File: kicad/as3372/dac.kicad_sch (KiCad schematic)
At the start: 6 parts, among them U13 LM4040AIM3-2.5, U14 AD5328

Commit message: incremental updates
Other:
- title: Zoxnoxious 3340 Oscillator -> Z3372 Signal Processing
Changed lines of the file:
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@@
   (paper "B")
   (title_block
-    (title "Zoxnoxious 3340 Oscillator")
-    (rev "0.4")
+    (title "Z3372 Signal Processing")
+    (rev "0.1")
     (company "Zoxnoxious Engineering")
   )

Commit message: progress
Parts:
- added C? (x2): 1n, Capacitor_SMD:C_0603_1608Metric, symbol Device:C
- added R? (x2): 2.4k, Resistor_SMD:R_0603_1608Metric, symbol Device:R
- added R? (x2): 120k, Resistor_SMD:R_0603_1608Metric, symbol Device:R
- added R? (x2): 3.3k, Resistor_SMD:R_0603_1608Metric, symbol Device:R
- added R? (x2): 8.2k, Resistor_SMD:R_0603_1608Metric, symbol Device:R
- added U? (x3): TL072, symbol Amplifier_Operational:TL072
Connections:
- net GND: now also C?.2, C?.2, R?.1, R?.1
- net VREF_2.5V: now also R?.1, R?.1
- net VCF_CV: now reaches U14.10 (VOUT_E)
- net VCF_CV: now also R?.1
- net PAN_VCA_CV: now reaches U14.11 (VOUT_F)
- net PAN_VCA_CV: now also R?.1
- net SIG1_VCA1_CV: now reaches U14.4 (VOUT_A)
- net SIG2_VCA2_CV: now reaches U14.5 (VOUT_B)
- net MOD_AMOUNT_VCA3_CV: now reaches U14.6 (VOUT_C)
- net RESONANCE_CV: now reaches U14.7 (VOUT_D)
- new net: C?.1, R?.2, R?.2, U?.5 (+)
- new net: R?.1, R?.2, U?.2 (-)
- new net: R?.2, U?.1
- new net: C?.1, R?.2, R?.2, U?.3 (+)
- new net: R?.1, R?.2, U?.6 (-)
- new net: R?.2, U?.7
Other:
- note added: "ADD SIMPLE RC FILTERING HERE"
- note added: "Control Voltage levels: Sig1 VCA CV: 0-5V Sig2 VCA CV: 0-5V VCA Mod Level CV: 0-5V Res CV: 0-5V VCF CV: -1 - +6V Pan VCA CV: -1 - +6V The latter two use opamps to scale; everything else can be straight from DAC"
- note added: "LM4040 resistor rough calc: Ilm4040 min: 70uA Vref input impedance: 10M"
- note removed: "LM4040 resistor rough calc: Ilm4040 min: 70uA Rdacref = 100k ==> I = 25uA opamp will swing about 0 ~{50} uA for roughly 150uA ==> 16kR min Lower to 5k, call it good"
- moved on the sheet: C24, C25, C39, R47, U13, U14

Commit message: daily update
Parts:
- removed U14: AD5328, Package_SO:TSSOP-16_4.4x5mm_P0.65mm, symbol as3340:AD5328
- removed U? (x3): TL072, symbol Amplifier_Operational:TL072
- added C7, C8: 0.1u, Capacitor_SMD:C_0603_1608Metric, symbol Device:C
- added TP14: TestPoint, symbol Connector:TestPoint
- added U4: TL074, symbol Amplifier_Operational:TL074
- added U9: AD5328, Package_SO:TSSOP-16_4.4x5mm_P0.65mm, symbol as3372_lib:AD5328
- C10, C9: renamed from C?; value 1n -> 68n; LCSC Part (none) -> C31658
- gave numbers to parts that had none: 8
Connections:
- net +5V: now also U9.3 (VDD)
- net DIN: now also U9.15 (DIN)
- net GND: now also C7.1, C8.1, U4.12 (+), U9.1 (~{LDAC}), U9.14 (GND)
- net MOD_AMOUNT_VCA3_CV: now also U9.6 (VOUT_C)
- net PAN_VCA_CV: now also R12.2, U4.1; no longer R6.1
- net RESONANCE_CV: now also U9.7 (VOUT_D)
- net SCLK: now also U9.16 (SCLK)
- net SIG1_VCA1_CV: now also U9.4 (VOUT_A)
- net SIG2_VCA2_CV: now also U9.5 (VOUT_B)
- net VCF_CV: now also R11.2, U4.7; no longer R5.1
- net VREF_2.5V: now also U4.10 (+), U9.8 (VREF_ABCD), U9.9 (VREF_EFGH); no longer R7.1, R8.1
- net ~{DAC_CS}: now also U9.2 (~{SYNC})
- net at C10.1, R10.2, R6.2: now also U4.3 (+)
- net at R11.1, R7.2: now also U4.6 (-)
- net at C9.1, R5.2, R9.2: now also U4.5 (+)
- net at R12.1, R8.2: now also U4.2 (-)
- new net: U4.13 (-), U4.14
- new net +12V: C7.2, U4.4 (V+)
- new net -12V: C8.2, U4.11 (V-)
- new net DAC_TEST: TP14.1, U9.13 (VOUT_H)
- new net PAN_VCA_CV_0-5: R6.1, U9.11 (VOUT_F)
- new net VCF_CV_0-5: R5.1, U9.10 (VOUT_E)
- new net VREF_2.5V_BUFFERED: R7.1, R8.1, U4.8, U4.9 (-)
- no-connect marks 0 -> 1
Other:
- note added: "Decoupling"
- note added: "Differential amplifier to take 0V : 5V to -1V : 6V 68nF cap to give a ~1kHz low pass filter"
- note added: "LM4040 resistor rough calc: Ilm4040 min: 70uA Vref input impedance: 10M (buffered)"
- note added: "Unused"
- note removed: "LM4040 resistor rough calc: Ilm4040 min: 70uA Vref input impedance: 10M"
- moved on the sheet: C10, C9, R10, R11, R12, R5, R6, R7, R8, R9

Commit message: schematic updates
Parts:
- R10, R9: LCSC Part (none) -> C25808
- R11, R12: LCSC Part (none) -> C22978
- R5, R6: LCSC Part (none) -> C22940
- R7, R8: LCSC Part (none) -> C25981
- TP14: footprint (none) -> TestPoint:TestPoint_Pad_2.0x2.0mm
- U4: footprint (none) -> Package_SO:SOIC-14_3.9x8.7mm_P1.27mm; LCSC Part (none) -> C6963
- U9: LCSC Part (none) -> C29162
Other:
- note added: "AD5328: "B" version works fine. DAC: 2.5V Reference Voltage B, C, D grades of LM4040 are likely good 'nuff"
- note removed: "DAC: 2.5V Reference Voltage B, C, D grades of LM4040 are likely good 'nuff"
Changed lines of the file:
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@@
     (effects (font (size 1.27 1.27)) (justify left bottom))
   )
-  (text "DAC: 2.5V Reference Voltage\nB, C, D grades of LM4040 are likely good 'nuff"
-    (at 24.765 24.13 0)
+  (text "AD5328: \"B\" version works fine.\nDAC: 2.5V Reference Voltage\nB, C, D grades of LM4040 are likely good 'nuff"
+    (at 24.765 27.305 0)
     (effects (font (size 1.27 1.27)) (justify left bottom))
   )
@@
     )
     (property "Datasheet" "https://www.analog.com/en/products/ad5308.html" (id 3) (at 76.2 57.15 0)
+      (effects (font (size 1.27 1.27)) hide)
+    )
+    (property "LCSC Part" "C29162" (id 4) (at 76.2 57.15 0)
       (effects (font (size 1.27 1.27)) hide)
     )
@@
       (effects (font (size 1.27 1.27)) (justify right))
     )
-    (property "Footprint" "" (id 2) (at 64.77 238.76 0)
+    (property "Footprint" "Package_SO:SOIC-14_3.9x8.7mm_P1.27mm" (id 2) (at 64.77 238.76 0)
       (effects (font (size 1.27 1.27)) hide)
     )
     (property "Datasheet" "http://www.ti.com/lit/ds/symlink/tl071.pdf" (id 3) (at 62.23 236.22 0)
+      (effects (font (size 1.27 1.27)) hide)
+    )
+    (property "LCSC Part" "C6963" (id 4) (at 63.5 241.3 0)
       (effects (font (size 1.27 1.27)) hide)
     )
@@
       (effects (font (size 1.27 1.27)) hide)
     )
+    (property "LCSC Part" "C22940" (id 4) (at 185.42 149.86 0)
+      (effects (font (size 1.27 1.27)) hide)
+    )
     (pin "1")
     (pin "2")
@@
     )
     (property "Datasheet" "~" (id 3) (at 190.5 157.48 0)
+      (effects (font (size 1.27 1.27)) hide)
+    )
+    (property "LCSC Part" "C25808" (id 4) (at 190.5 157.48 0)
       (effects (font (size 1.27 1.27)) hide)
     )
@@
       (effects (font (size 1.27 1.27)) hide)
     )
+    (property "LCSC Part" "C22978" (id 4) (at 207.01 90.17 0)
+      (effects (font (size 1.27 1.27)) hide)
+    )
     (pin "1")
     (pin "2")
@@
     (property "Reference" "U4" (id 0) (at 207.01 94.0902 0))
     (property "Value" "TL074" (id 1) (at 207.01 96.6271 0))
-    (property "Footprint" "" (id 2) (at 205.74 105.41 0)
+    (property "Footprint" "Package_SO:SOIC-14_3.9x8.7mm_P1.27mm" (id 2) (at 205.74 105.41 0)
       (effects (font (size 1.27 1.27)) hide)
     )
     (property "Datasheet" "http://www.ti.com/lit/ds/symlink/tl071.pdf" (id 3) (at 208.28 107.95 0)
+      (effects (font (size 1.27 1.27)) hide)
+    )
+    (property "LCSC Part" "C6963" (id 4) (at 207.01 102.87 0)
       (effects (font (size 1.27 1.27)) hide)
     )
@@
       (effects (font (size 1.27 1.27)) hide)
     )
+    (property "LCSC Part" "C25981" (id 4) (at 189.23 100.33 0)
+      (effects (font (size 1.27 1.27)) hide)
+    )
     (pin "1")
     (pin "2")
@@
     (property "Reference" "U4" (id 0) (at 205.74 58.5302 0))
     (property "Value" "TL074" (id 1) (at 205.74 61.0671 0))
-    (property "Footprint" "" (id 2) (at 204.47 69.85 0)
+    (property "Footprint" "Package_SO:SOIC-14_3.9x8.7mm_P1.27mm" (id 2) (at 204.47 69.85 0)
       (effects (font (size 1.27 1.27)) hide)
     )
     (property "Datasheet" "http://www.ti.com/lit/ds/symlink/tl071.pdf" (id 3) (at 207.01 72.39 0)
+      (effects (font (size 1.27 1.27)) hide)
+    )
+    (property "LCSC Part" "C6963" (id 4) (at 205.74 67.31 0)
       (effects (font (size 1.27 1.27)) hide)
     )
@@
     (property "Reference" "U4" (id 0) (at 383.54 200.7702 0))
     (property "Value" "TL074" (id 1) (at 383.54 203.3071 0))
-    (property "Footprint" "" (id 2) (at 382.27 212.09 0)
+    (property "Footprint" "Package_SO:SOIC-14_3.9x8.7mm_P1.27mm" (id 2) (at 382.27 212.09 0)
       (effects (font (size 1.27 1.27)) hide)
     )
     (property "Datasheet" "http://www.ti.com/lit/ds/symlink/tl071.pdf" (id 3) (at 384.81 214.63 0)
+      (effects (font (size 1.27 1.27)) hide)
+    )
+    (property "LCSC Part" "C6963" (id 4) (at 383.54 209.55 0)
       (effects (font (size 1.27 1.27)) hide)
     )
@@
     (property "Reference" "U4" (id 0) (at 207.01 138.5402 0))
     (property "Value" "TL074" (id 1) (at 207.01 141.0771 0))
-    (property "Footprint" "" (id 2) (at 205.74 149.86 0)
+    (property "Footprint" "Package_SO:SOIC-14_3.9x8.7mm_P1.27mm" (id 2) (at 205.74 149.86 0)
       (effects (font (size 1.27 1.27)) hide)
     )
     (property "Datasheet" "http://www.ti.com/lit/ds/symlink/tl071.pdf" (id 3) (at 208.28 152.4 0)
+      (effects (font (size 1.27 1.27)) hide)
+    )
+    (property "LCSC Part" "C6963" (id 4) (at 207.01 147.32 0)
       (effects (font (size 1.27 1.27)) hide)
     )
@@
       (effects (font (size 1.27 1.27)) hide)
     )
+    (property "LCSC Part" "C22978" (id 4) (at 207.01 134.62 0)
+      (effects (font (size 1.27 1.27)) hide)
+    )
     (pin "1")
     (pin "2")
@@
       (effects (font (size 1.27 1.27)) (justify left))
     )
-    (property "Footprint" "" (id 2) (at 105.41 72.39 0)
+    (property "Footprint" "TestPoint:TestPoint_Pad_2.0x2.0mm" (id 2) (at 105.41 72.39 0)
       (effects (font (size 1.27 1.27)) hide)
     )
@@
       (effects (font (size 1.27 1.27)) hide)
     )
+    (property "LCSC Part" "C22940" (id 4) (at 185.42 105.41 0)
+      (effects (font (size 1.27 1.27)) hide)
+    )
     (pin "1")
     (pin "2")
@@
       (effects (font (size 1.27 1.27)) hide)
     )
+    (property "LCSC Part" "C25808" (id 4) (at 190.5 113.03 0)
+      (effects (font (size 1.27 1.27)) hide)
+    )
     (pin "1")
     (pin "2")
@@
       (effects (font (size 1.27 1.27)) hide)
     )
+    (property "LCSC Part" "C25981" (id 4) (at 189.23 144.78 0)
+      (effects (font (size 1.27 1.27)) hide)
+    )

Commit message: start placing
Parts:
- added C41, C42, C43, C44: 10n, Capacitor_SMD:C_0603_1608Metric, symbol Device:C
- added R74, R75, R76, R77: 15k, Resistor_SMD:R_0603_1608Metric, symbol Device:R
- C10: value 68n -> 8.2p; LCSC Part C31658 -> C1685
- R10: value 120k -> 20k; LCSC Part C25808 -> C4184
- R12: value 3.3k -> 20k; LCSC Part C22978 -> C4184
- R6: value 2.4k -> 20k; LCSC Part C22940 -> C4184
- R8: value 8.2k -> 20k; LCSC Part C25981 -> C4184
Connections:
- net GND: now also C41.2, C42.2, C43.2, C44.2
- net MOD_AMOUNT_VCA3_CV: now also C43.1, R76.2; no longer U9.6 (VOUT_C)
- net RESONANCE_CV: now also C44.1, R77.2; no longer U9.7 (VOUT_D)
- net SIG1_VCA1_CV: now also C41.1, R74.2; no longer U9.4 (VOUT_A)
- net SIG2_VCA2_CV: now also C42.1, R75.2; no longer U9.5 (VOUT_B)
- net PAN_VCA_CV_0-5 renamed PAN_VCA_CV_DAC
- net VCF_CV_0-5 renamed VCF_CV_DAC
- new net MOD_AMOUNT_VCA3_DAC: R76.1, U9.6 (VOUT_C)
- new net RESONANCE_DAC: R77.1, U9.7 (VOUT_D)
- new net SIG1_VCA_DAC: R74.1, U9.4 (VOUT_A)
- new net SIG2_VCA_DAC: R75.1, U9.5 (VOUT_B)
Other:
- note added: "Control Voltage levels: Sig1 VCA CV: 0-5V Sig2 VCA CV: 0-5V VCA Mod Level CV: 0-5V Res CV: 0-5V VCF CV: -1 - +6V Pan VCA CV: -2.5 - +2.5V The latter two use opamps to scale; everything else can be straight from DAC. These are slightly outside datasheet specs of 0:5 and -2:+2 to allow for some offset from modulation."
- note added: "Pan CVA CV: Take 0V : 5V from DAC shift to -2.5V : 2.5V output 8.2p cap to give a ~1kHz low pass filter"
- note added: "RC lowpass at ~1kHz"
- note added: "VCF Cutoff CV: Take 0V : 5V from DAC shift to -1V : 6V output 68nF cap to give a ~1kHz low pass filter"
- note removed: "Control Voltage levels: Sig1 VCA CV: 0-5V Sig2 VCA CV: 0-5V VCA Mod Level CV: 0-5V Res CV: 0-5V VCF CV: -1 - +6V Pan VCA CV: -1 - +6V The latter two use opamps to scale; everything else can be straight from DAC"
- note removed: "Differential amplifier to take 0V : 5V to -1V : 6V 68nF cap to give a ~1kHz low pass filter"
- moved on the sheet: C10, C7, C8, C9, R10, R11, R12, R5, R6, R7, R8, R9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

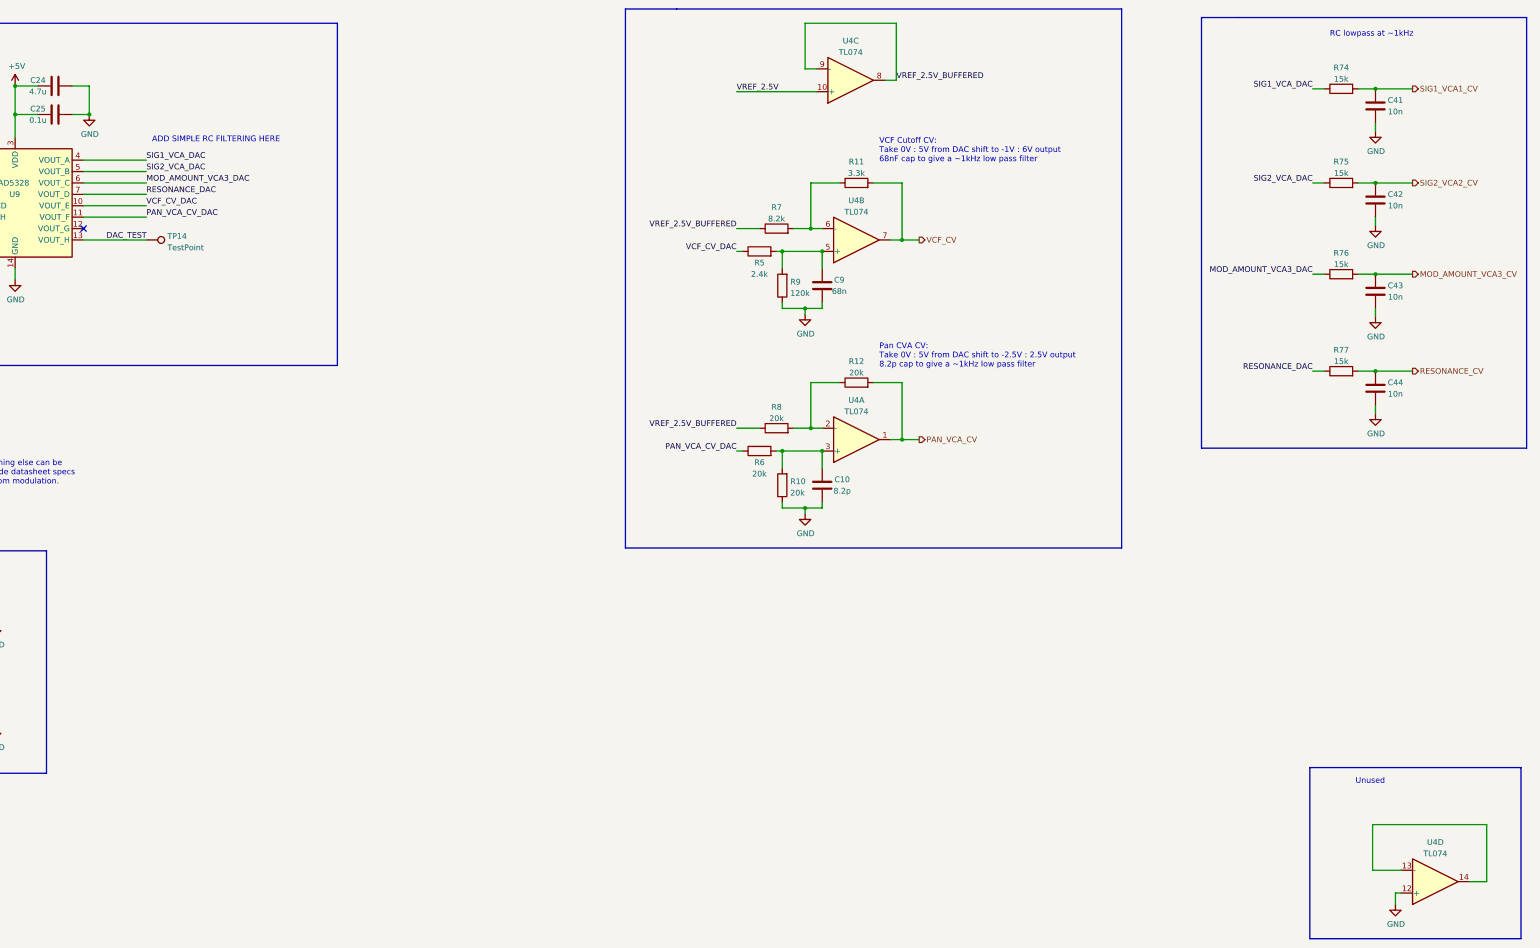
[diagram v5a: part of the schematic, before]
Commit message: starting routing...which may be detrimental
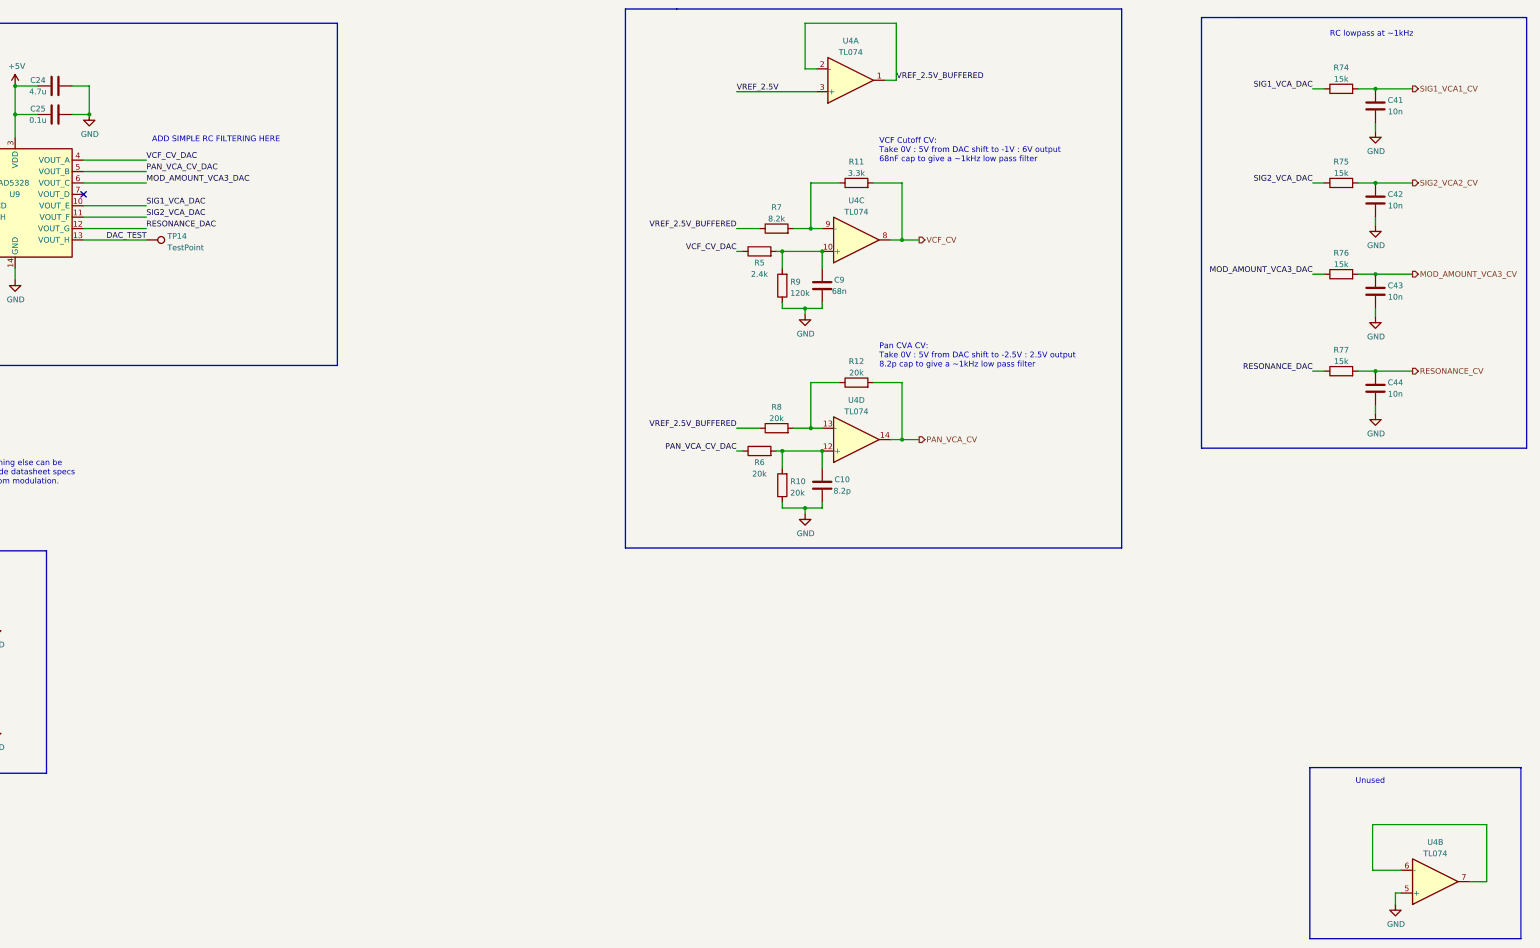
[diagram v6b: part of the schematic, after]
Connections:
- net GND: now also U4.5 (+); no longer U4.12 (+)
- net PAN_VCA_CV: now also U4.14; no longer U4.1
- net PAN_VCA_CV_DAC: now also U9.5 (VOUT_B); no longer U9.11 (VOUT_F)
- net RESONANCE_DAC: now also U9.12 (VOUT_G); no longer U9.7 (VOUT_D)
- net SIG1_VCA_DAC: now also U9.10 (VOUT_E); no longer U9.4 (VOUT_A)
- net SIG2_VCA_DAC: now also U9.11 (VOUT_F); no longer U9.5 (VOUT_B)
- net VCF_CV: now also U4.8; no longer U4.7
- net VCF_CV_DAC: now also U9.4 (VOUT_A); no longer U9.10 (VOUT_E)
- net VREF_2.5V: now also U4.3 (+); no longer U4.10 (+)
- net VREF_2.5V_BUFFERED: now also U4.1, U4.2 (-); no longer U4.8, U4.9 (-)
- net at C10.1, R10.2, R6.2: now also U4.12 (+); no longer U4.3 (+)
- net at R11.1, R7.2: now also U4.9 (-); no longer U4.6 (-)
- net at C9.1, R5.2, R9.2: now also U4.10 (+); no longer U4.5 (+)
- net at R12.1, R8.2: now also U4.13 (-); no longer U4.2 (-)
- new net: U4.6 (-), U4.7

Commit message: routing done needs review
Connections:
- net DAC_TEST: now also U9.6 (VOUT_C); no longer U9.13 (VOUT_H)
- net MOD_AMOUNT_VCA3_DAC: now also U9.7 (VOUT_D); no longer U9.6 (VOUT_C)
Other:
- moved on the sheet: TP14
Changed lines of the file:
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@@
   (junction (at 61.595 173.355) (diameter 0) (color 0 0 0 0)
   )
-  (no_connect (at 91.44 57.15))
+  (no_connect (at 91.44 67.31))
   (wire (pts (xy 247.015 81.28) (xy 247.015 82.55))
     (stroke (width 0) (type default) (color 0 0 0 0))
@@
     (stroke (width 0) (type default) (color 0 0 0 0))
   )
-  (wire (pts (xy 91.44 54.61) (xy 105.41 54.61))
+  (wire (pts (xy 91.44 57.15) (xy 105.41 57.15))
     (stroke (width 0) (type default) (color 0 0 0 0))
   )
@@
     (stroke (width 0) (type default) (color 0 0 0 0))
   )
-  (wire (pts (xy 91.44 67.31) (xy 105.41 67.31))
+  (wire (pts (xy 91.44 54.61) (xy 129.54 54.61))
     (stroke (width 0) (type default) (color 0 0 0 0))
   )
@@
     (effects (font (size 1.27 1.27)) (justify right bottom))
   )
-  (label "MOD_AMOUNT_VCA3_DAC" (at 105.41 54.61 0)
-    (effects (font (size 1.27 1.27)) (justify left bottom))
-  )
-  (label "DAC_TEST" (at 96.52 67.31 0)
+  (label "MOD_AMOUNT_VCA3_DAC" (at 105.41 57.15 0)
+    (effects (font (size 1.27 1.27)) (justify left bottom))
+  )
+  (label "DAC_TEST" (at 96.52 54.61 0)
     (effects (font (size 1.27 1.27)) (justify left bottom))
   )
@@
     (pin "2")
   )
-  (symbol (lib_id "Connector:TestPoint") (at 105.41 67.31 270) (unit 1)
-    (in_bom yes) (on_board yes) (fields_autoplaced)
-    (property "Reference" "TP14" (id 0) (at 110.109 66.4753 90)
+  (symbol (lib_id "Connector:TestPoint") (at 129.54 54.61 270) (unit 1)
+    (in_bom yes) (on_board yes) (fields_autoplaced)
+    (property "Reference" "TP14" (id 0) (at 134.239 53.7753 90)
       (effects (font (size 1.27 1.27)) (justify left))
     )
-    (property "Value" "TestPoint" (id 1) (at 110.109 69.0122 90)
+    (property "Value" "TestPoint" (id 1) (at 134.239 56.3122 90)
       (effects (font (size 1.27 1.27)) (justify left))
     )
-    (property "Footprint" "TestPoint:TestPoint_Pad_2.0x2.0mm" (id 2) (at 105.41 72.39 0)
-      (effects (font (size 1.27 1.27)) hide)
-    )
-    (property "Datasheet" "~" (id 3) (at 105.41 72.39 0)
-      (effects (font (size 1.27 1.27)) hide)
-    )
+    (property "Footprint" "TestPoint:TestPoint_Pad_2.0x2.0mm" (id 2) (at 129.54 59.69 0)
+      (effects (font (size 1.27 1.27)) hide)
+    )
+    (property "Datasheet" "~" (id 3) (at 129.54 59.69 0)
+      (effects (font (size 1.27 1.27)) hide)
+    )
